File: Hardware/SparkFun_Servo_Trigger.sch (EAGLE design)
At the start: 30 parts, among them U1 ATTINY84, Y1 16MHZ

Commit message: changed micro fids to regular size
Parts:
- FID1, FID2: value FIDUCIALUFIDUCIAL -> FIDUCIAL1X2; device SparkFun-Aesthetics:FIDUCIALUFIDUCIAL -> SparkFun-Aesthetics:FIDUCIAL1X2
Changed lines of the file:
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@@
 <?xml version="1.0" encoding="utf-8"?>
 <!DOCTYPE eagle SYSTEM "eagle.dtd">
-<eagle version="7.1.0">
+<eagle version="6.6.0">
 <drawing>
 <settings>
@@
 <grid distance="0.1" unitdist="inch" unit="inch" style="lines" multiple="1" display="no" altdistance="0.01" altunitdist="inch" altunit="inch"/>
 <layers>
-<layer number="1" name="Top" color="4" fill="1" visible="yes" active="no"/>
-<layer number="2" name="Route2" color="1" fill="3" visible="yes" active="no"/>
-<layer number="3" name="Route3" color="4" fill="3" visible="yes" active="no"/>
-<layer number="4" name="Route4" color="1" fill="4" visible="yes" active="no"/>
-<layer number="5" name="Route5" color="4" fill="4" visible="yes" active="no"/>
-<layer number="6" name="Route6" color="1" fill="8" visible="yes" active="no"/>
-<layer number="7" name="Route7" color="4" fill="8" visible="yes" active="no"/>
-<layer number="8" name="Route8" color="1" fill="2" visible="yes" active="no"/>
-<layer number="9" name="Route9" color="4" fill="2" visible="yes" active="no"/>
-<layer number="10" name="Route10" color="1" fill="7" visible="yes" active="no"/>
-<layer number="11" name="Route11" color="4" fill="7" visible="yes" active="no"/>
-<layer number="12" name="Route12" color="1" fill="5" visible="yes" active="no"/>
-<layer number="13" name="Route13" color="4" fill="5" visible="yes" active="no"/>
-<layer number="14" name="Route14" color="1" fill="6" visible="yes" active="no"/>
-<layer number="15" name="Route15" color="4" fill="6" visible="yes" active="no"/>
-<layer number="16" name="Bottom" color="1" fill="1" visible="yes" active="no"/>
-<layer number="17" name="Pads" color="2" fill="1" visible="yes" active="no"/>
-<layer number="18" name="Vias" color="2" fill="1" visible="yes" active="no"/>
-<layer number="19" name="Unrouted" color="6" fill="1" visible="yes" active="no"/>
-<layer number="20" name="Dimension" color="15" fill="1" visible="yes" active="no"/>
-<layer number="21" name="tPlace" color="16" fill="1" visible="yes" active="no"/>
-<layer number="22" name="bPlace" color="14" fill="1" visible="yes" active="no"/>
-<layer number="23" name="tOrigins" color="15" fill="1" visible="yes" active="no"/>
-<layer number="24" name="bOrigins" color="15" fill="1" visible="yes" active="no"/>
-<layer number="25" name="tNames" color="7" fill="1" visible="yes" active="no"/>
-<layer number="26" name="bNames" color="7" fill="1" visible="yes" active="no"/>
-<layer number="27" name="tValues" color="7" fill="1" visible="yes" active="no"/>
-<layer number="28" name="bValues" color="7" fill="1" visible="yes" active="no"/>
+<layer number="1" name="Top" color="4" fill="1" visible="no" active="no"/>
+<layer number="2" name="Route2" color="1" fill="3" visible="no" active="no"/>
+<layer number="3" name="Route3" color="4" fill="3" visible="no" active="no"/>
+<layer number="4" name="Route4" color="1" fill="4" visible="no" active="no"/>
+<layer number="5" name="Route5" color="4" fill="4" visible="no" active="no"/>
+<layer number="6" name="Route6" color="1" fill="8" visible="no" active="no"/>
+<layer number="7" name="Route7" color="4" fill="8" visible="no" active="no"/>
+<layer number="8" name="Route8" color="1" fill="2" visible="no" active="no"/>
+<layer number="9" name="Route9" color="4" fill="2" visible="no" active="no"/>
+<layer number="10" name="Route10" color="1" fill="7" visible="no" active="no"/>
+<layer number="11" name="Route11" color="4" fill="7" visible="no" active="no"/>
+<layer number="12" name="Route12" color="1" fill="5" visible="no" active="no"/>
+<layer number="13" name="Route13" color="4" fill="5" visible="no" active="no"/>
+<layer number="14" name="Route14" color="1" fill="6" visible="no" active="no"/>
+<layer number="15" name="Route15" color="4" fill="6" visible="no" active="no"/>
+<layer number="16" name="Bottom" color="1" fill="1" visible="no" active="no"/>
+<layer number="17" name="Pads" color="2" fill="1" visible="no" active="no"/>
+<layer number="18" name="Vias" color="2" fill="1" visible="no" active="no"/>
+<layer number="19" name="Unrouted" color="6" fill="1" visible="no" active="no"/>
+<layer number="20" name="Dimension" color="15" fill="1" visible="no" active="no"/>
+<layer number="21" name="tPlace" color="16" fill="1" visible="no" active="no"/>
+<layer number="22" name="bPlace" color="14" fill="1" visible="no" active="no"/>
+<layer number="23" name="tOrigins" color="15" fill="1" visible="no" active="no"/>
+<layer number="24" name="bOrigins" color="15" fill="1" visible="no" active="no"/>
+<layer number="25" name="tNames" color="7" fill="1" visible="no" active="no"/>
+<layer number="26" name="bNames" color="7" fill="1" visible="no" active="no"/>
+<layer number="27" name="tValues" color="7" fill="1" visible="no" active="no"/>
+<layer number="28" name="bValues" color="7" fill="1" visible="no" active="no"/>
 <layer number="29" name="tStop" color="7" fill="3" visible="no" active="no"/>
 <layer number="30" name="bStop" color="7" fill="6" visible="no" active="no"/>
@@
 <layer number="35" name="tGlue" color="7" fill="4" visible="no" active="no"/>
 <layer number="36" name="bGlue" color="7" fill="5" visible="no" active="no"/>
-<layer number="37" name="tTest" color="7" fill="1" visible="yes" active="no"/>
-<layer number="38" name="bTest" color="7" fill="1" visible="yes" active="no"/>
+<layer number="37" name="tTest" color="7" fill="1" visible="no" active="no"/>
+<layer number="38" name="bTest" color="7" fill="1" visible="no" active="no"/>
 <layer number="39" name="tKeepout" color="4" fill="11" visible="no" active="no"/>
 <layer number="40" name="bKeepout" color="1" fill="11" visible="no" active="no"/>
@@
 <layer number="44" name="Drills" color="7" fill="1" visible="no" active="no"/>
 <layer number="45" name="Holes" color="7" fill="1" visible="no" active="no"/>
-<layer number="46" name="Milling" color="3" fill="1" visible="yes" active="no"/>
-<layer number="47" name="Measures" color="7" fill="1" visible="yes" active="no"/>
-<layer number="48" name="Document" color="7" fill="1" visible="yes" active="no"/>
-<layer number="49" name="Reference" color="7" fill="1" visible="yes" active="no"/>
-<layer number="50" name="dxf" color="7" fill="1" visible="yes" active="no"/>
-<layer number="51" name="tDocu" color="6" fill="1" visible="yes" active="no"/>
-<layer number="52" name="bDocu" color="7" fill="1" visible="yes" active="no"/>
-<layer number="53" name="tGND_GNDA" color="7" fill="9" visible="yes" active="no"/>
-<layer number="54" name="bGND_GNDA" color="1" fill="9" visible="yes" active="no"/>
-<layer number="56" name="wert" color="7" fill="1" visible="yes" active="no"/>
-<layer number="57" name="tCAD" color="7" fill="1" visible="yes" active="no"/>
+<layer number="46" name="Milling" color="3" fill="1" visible="no" active="no"/>
+<layer number="47" name="Measures" color="7" fill="1" visible="no" active="no"/>
+<layer number="48" name="Document" color="7" fill="1" visible="no" active="no"/>
+<layer number="49" name="Reference" color="7" fill="1" visible="no" active="no"/>
+<layer number="50" name="dxf" color="7" fill="1" visible="no" active="no"/>
+<layer number="51" name="tDocu" color="6" fill="1" visible="no" active="no"/>
+<layer number="52" name="bDocu" color="7" fill="1" visible="no" active="no"/>
+<layer number="53" name="tGND_GNDA" color="7" fill="9" visible="no" active="no"/>
+<layer number="54" name="bGND_GNDA" color="1" fill="9" visible="no" active="no"/>
+<layer number="56" name="wert" color="7" fill="1" visible="no" active="no"/>
+<layer number="57" name="tCAD" color="7" fill="1" visible="no" active="no"/>
 <layer number="90" name="Modules" color="5" fill="1" visible="yes" active="yes"/>
 <layer number="91" name="Nets" color="2" fill="1" visible="yes" active="yes"/>
@@
 <part name="LOGO1" library="SparkFun-Aesthetics" deviceset="OSHW-LOGO" device="M"/>
 <part name="LOGO2" library="SparkFun-Aesthetics" deviceset="SFE_LOGO_NAME" device=".2_INCH"/>
-<part name="FID1" library="SparkFun-Aesthetics" deviceset="FIDUCIAL" device="UFIDUCIAL"/>
-<part name="FID2" library="SparkFun-Aesthetics" deviceset="FIDUCIAL" device="UFIDUCIAL"/>
 <part name="R5" library="SparkFun-Resistors" deviceset="10KOHM-1/10W-1%(0603)" device="0603" value="10K"/>
 <part name="SUPPLY11" library="SparkFun-Aesthetics" deviceset="VCC" device=""/>
@@
 <part name="TP2" library="SparkFun-Passives" deviceset="TEST-POINT" device="3X4" value="TEST-POINT3X4"/>
 <part name="TP3" library="SparkFun-Passives" deviceset="TEST-POINT" device="3X4" value="TEST-POINT3X4"/>
+<part name="FID1" library="SparkFun-Aesthetics" deviceset="FIDUCIAL" device="1X2"/>
+<part name="FID2" library="SparkFun-Aesthetics" deviceset="FIDUCIAL" device="1X2"/>
 </parts>
 <sheets>
@@
 <instance part="LOGO1" gate="G$1" x="160.02" y="45.72"/>
 <instance part="LOGO2" gate="G$1" x="190.5" y="35.56"/>
-<instance part="FID1" gate="G$1" x="246.38" y="17.78"/>
-<instance part="FID2" gate="G$1" x="243.84" y="17.78"/>
 <instance part="R5" gate="G$1" x="7.62" y="33.02" smashed="yes" rot="MR90">
 <attribute name="NAME" x="5.842" y="31.496" size="1.778" layer="95" rot="R90"/>
@@
 <attribute name="NAME" x="228.6" y="86.106" size="1.778" layer="95"/>
 </instance>
+<instance part="FID1" gate="G$1" x="243.84" y="17.78"/>
+<instance part="FID2" gate="G$1" x="246.38" y="17.78"/>
 </instances>
 <busses>

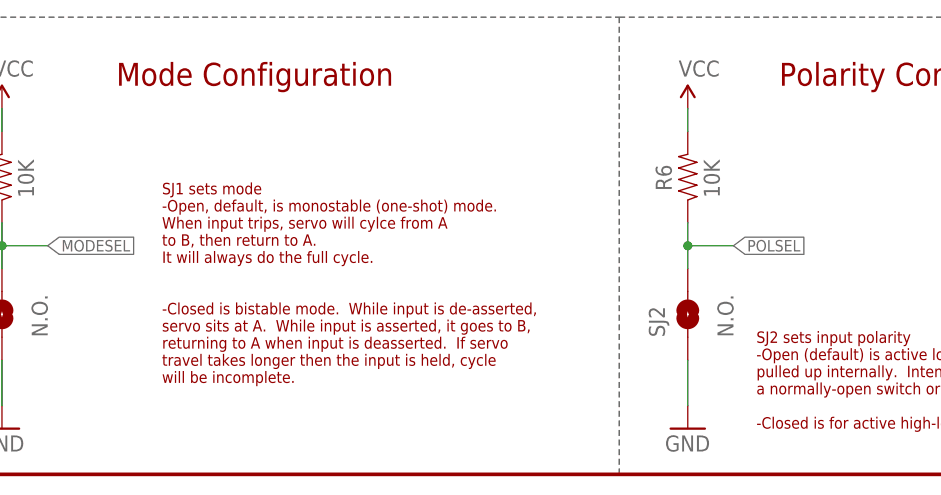
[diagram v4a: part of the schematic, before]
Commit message: Updating description of mode jumper.
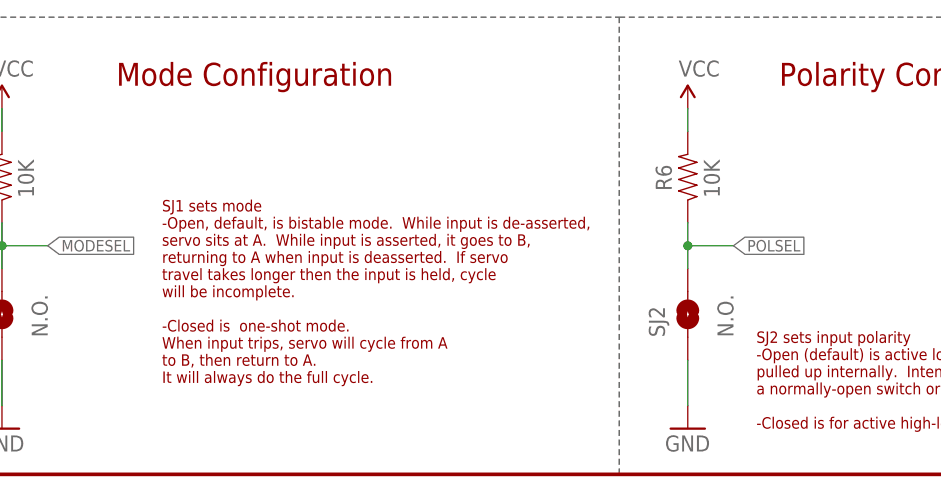
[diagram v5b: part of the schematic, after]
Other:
- note added: "SJ1 sets mode -Open, default, is bistable mode. While input is de-asserted, servo sits at A. While input is asserted, it goes to B, returning to A when input is deasserted. If servo travel takes longer then the input is held, cycle will be incomplete. -Closed is one-shot mode. When input trips, servo will cycle from A to B, then return to A. It will always do the full cycle."
- note removed: "SJ1 sets mode -Open, default, is monostable (one-shot) mode. When input trips, servo will cylce from A to B, then return to A. It will always do the full cycle. -Closed is bistable mode. While input is de-asserted, servo sits at A. While input is asserted, it goes to B, returning to A when input is deasserted. If servo travel takes longer then the input is held, cycle will be incomplete."
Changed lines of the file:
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@@
 <?xml version="1.0" encoding="utf-8"?>
 <!DOCTYPE eagle SYSTEM "eagle.dtd">
-<eagle version="6.6.0">
+<eagle version="7.3.0">
 <drawing>
 <settings>
@@
 <text x="93.98" y="43.18" size="2.54" layer="94" font="vector">Polarity Configuration</text>
 <text x="25.4" y="10.16" size="1.27" layer="94">SJ1 sets mode
--Open, default, is monostable (one-shot) mode.
-When input trips, servo will cylce from A
-to B, then return to A.
-It will always do the full cycle.
--Closed is bistable mode.  While input is de-asserted,
+-Open, default, is bistable mode.  While input is de-asserted,
 servo sits at A.  While input is asserted, it goes to B,
 returning to A when input is deasserted.  If servo
 travel takes longer then the input is held, cycle
-will be incomplete.</text>
+will be incomplete.
+-Closed is  one-shot mode.
+When input trips, servo will cycle from A
+to B, then return to A.
+It will always do the full cycle.</text>
 <text x="91.44" y="5.08" size="1.27" layer="94">SJ2 sets input polarity
 -Open (default) is active low, with switch input

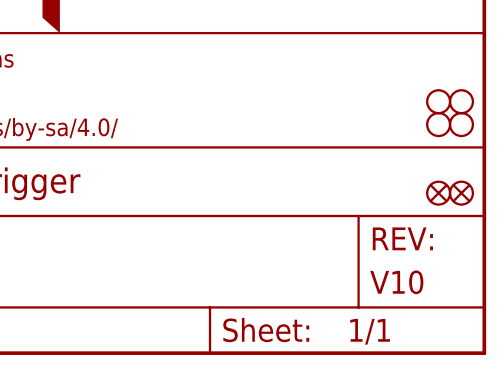
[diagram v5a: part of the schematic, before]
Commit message: Checking in V1.1 revision
Adding silkscreen tickboxes for standard/continuous rotation.

Moving to "STANDARD" DRC.
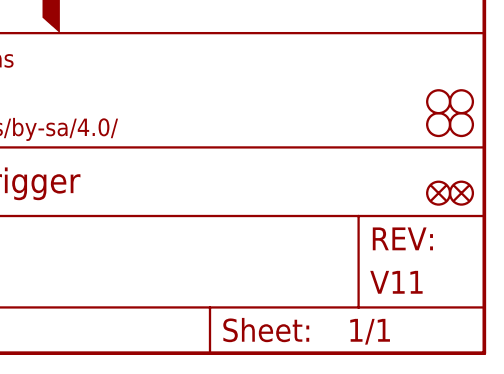
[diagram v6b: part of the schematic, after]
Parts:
- FRAME1: VERSION V10 -> V11
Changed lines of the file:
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@@
 <part name="FRAME1" library="SparkFun-Aesthetics" deviceset="FRAME-LETTER" device="">
 <attribute name="DESIGNER" value="Byron Jacquot"/>
-<attribute name="VERSION" value="V10"/>
+<attribute name="VERSION" value="V11"/>
 </part>
 <part name="R4" library="SparkFun-Resistors" deviceset="10KOHM-1/10W-1%(0603)" device="0603" value="10K"/>

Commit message: Updates from checklist.
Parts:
- FRAME1: value (none) -> frame
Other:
- note added: "For continuous rotation servo trigger: "A" sets the default speed & direction if the servo. "B" sets the alternate speed & direction. "T" sets the time it takes to move from A to B and back, over a range of 0 to 10 seconds."
- note added: "SJ1 sets mode Variant of servo trigger is indicated in a check-box on that back of the PCB. For "standard" servo trigger: -Open, default, is bistable mode. While input is de-asserted, servo sits at A. While input is asserted, it goes to B, returning to A when input is deasserted. If servo travel takes longer then the input is held, cycle will be incomplete. -Closed is one-shot mode. When input tr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"
- note added: "These pots control the servo position and timing. For standard servo trigger: "A" sets the default position if the servo. "B" sets the position it travels to when the switch is actuated (whether it stays there or not is configured with the mode jumper). "T" sets the time it takes to move from A to B and back, over a range of 0 to 10 seconds."
- note removed: "SJ1 sets mode -Open, default, is bistable mode. While input is de-asserted, servo sits at A. While input is asserted, it goes to B, returning to A when input is deasserted. If servo travel takes longer then the input is held, cycle will be incomplete. -Closed is one-shot mode. When input trips, servo will cycle from A to B, then return to A. It will always do the full cycle."
- note removed: "These pots control the servo position and timing. "A" sets the default position if the servo. "B" sets the position it travels to when the switch is actuated (whether it stays there or not is configured with the mode jumper). "T" sets the time it takes to move from A to B and back, over a range of 0 to 10 seconds."
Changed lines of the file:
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@@
 </classes>
 <parts>
-<part name="FRAME1" library="SparkFun-Aesthetics" deviceset="FRAME-LETTER" device="">
+<part name="FRAME1" library="SparkFun-Aesthetics" deviceset="FRAME-LETTER" device="" value="frame">
 <attribute name="DESIGNER" value="Byron Jacquot"/>
 <attribute name="VERSION" value="V11"/>
@@
 <text x="20.32" y="43.18" size="2.54" layer="94" font="vector">Mode Configuration</text>
 <text x="93.98" y="43.18" size="2.54" layer="94" font="vector">Polarity Configuration</text>
-<text x="25.4" y="10.16" size="1.27" layer="94">SJ1 sets mode
+<text x="25.4" y="5.08" size="1.27" layer="97">SJ1 sets mode
+Variant of servo trigger is indicated in a
+check-box on that back of the PCB.
+For "standard" servo trigger:
 -Open, default, is bistable mode.  While input is de-asserted,
 servo sits at A.  While input is asserted, it goes to B,
@@
 When input trips, servo will cycle from A
 to B, then return to A.
-It will always do the full cycle.</text>
-<text x="91.44" y="5.08" size="1.27" layer="94">SJ2 sets input polarity
+It will always do the full cycle.
+For "continuous rotoation" servo trigger
+-Open selects toggling mode.  On each actuation of input,
+trigger will switch to the other state - from A to B, or B to A.
+-Closed selects bistable, same as the default for standard
+Servo Trigger, as described above.</text>
+<text x="91.44" y="5.08" size="1.27" layer="97">SJ2 sets input polarity
 -Open (default) is active low, with switch input
 pulled up internally.  Intended for use with
 a normally-open switch or active-low logic.
 -Closed is for active high-logic.</text>
-<text x="124.46" y="139.7" size="1.27" layer="94">Pulled up internally in processor
+<text x="124.46" y="139.7" size="1.27" layer="97">Pulled up internally in processor
 Datasheet says Rup is in the 20K to 50K range.</text>
-<text x="5.08" y="139.7" size="1.27" layer="94">Expecting 5VDC power.
+<text x="5.08" y="139.7" size="1.27" layer="97">Expecting 5VDC power.
 Current consumed is dependent
 on servo type and loading.</text>
-<text x="154.94" y="53.34" size="1.27" layer="94">These pots control the servo position and timing.
+<text x="154.94" y="53.34" size="1.27" layer="97">These pots control the servo position and timing.
+For standard servo trigger:
 "A" sets the default position if the servo.
 "B" sets the position it travels to when the switch
@@
 "T" sets the time it takes to move from A to B
  and back, over a range of 0 to 10 seconds.</text>
+<text x="195.58" y="55.88" size="1.27" layer="97">For continuous rotation servo trigger:
+"A" sets the default speed &amp; direction if the servo.
+"B" sets the alternate speed &amp; direction.
+"T" sets the time it takes to move from A to B
+ and back, over a range of 0 to 10 seconds.</text>
